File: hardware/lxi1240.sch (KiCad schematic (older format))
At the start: 1 part

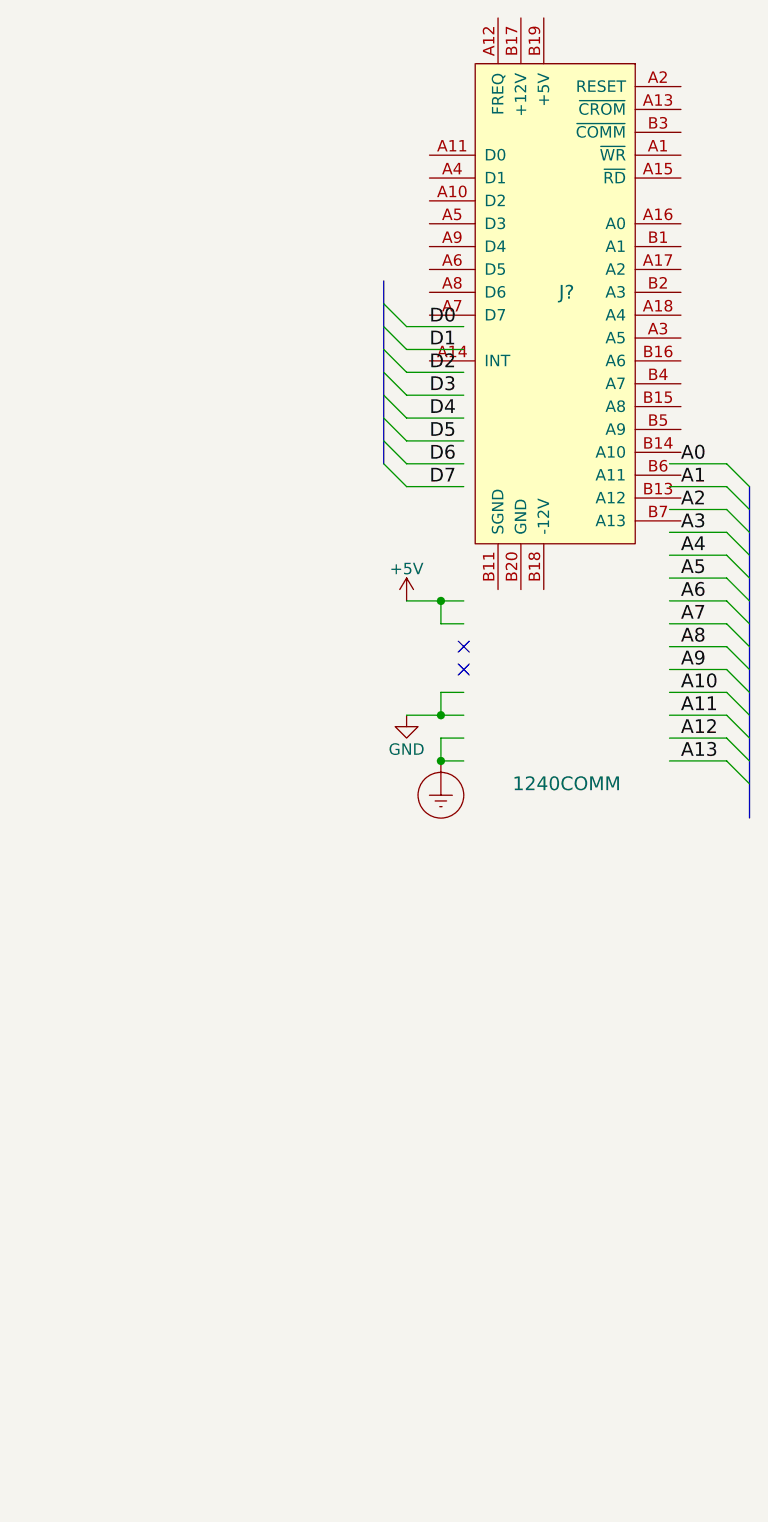
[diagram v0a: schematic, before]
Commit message: Make board-edge symbol compliant with KLC.
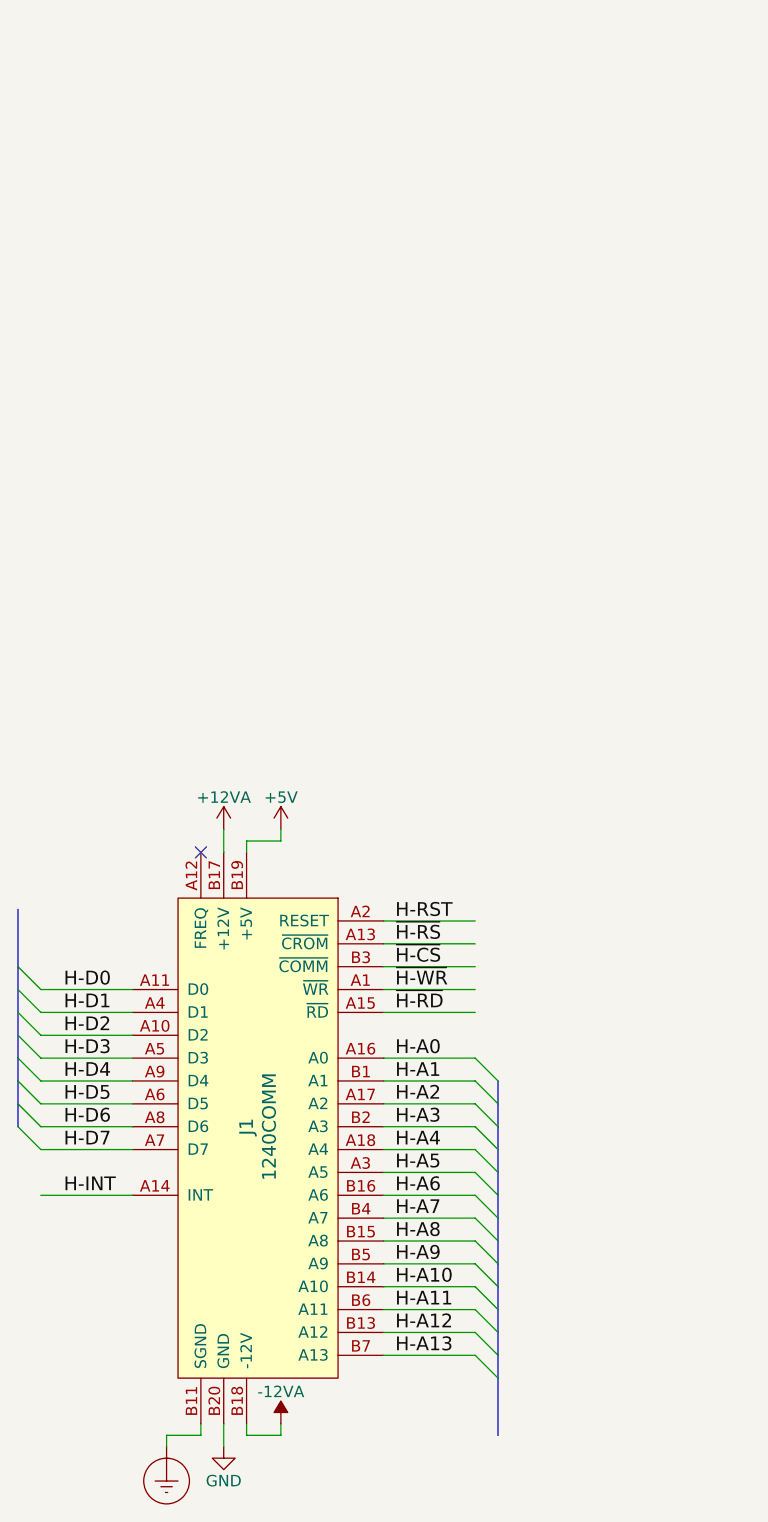
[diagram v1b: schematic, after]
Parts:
- removed J?: 1240COMM, symbol 1240COMM
- added J1: 1240COMM, symbol 1240COMM
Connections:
- net labels added: +12VA, -12VA, H-A0, H-A1, H-A10, H-A11, H-A12, H-A13, H-A2, H-A3, H-A4, H-A5, H-A6, H-A7, H-A8, H-A9, H-D0, H-D1, H-D2, H-D3, H-D4, H-D5, H-D6, H-D7, H-INT, H-RST, ~H-CS, ~H-RD, ~H-RS, ~H-WR
- net labels removed: A0, A1, A10, A11, A12, A13, A2, A3, A4, A5, A6, A7, A8, A9, D0, D1, D2, D3, D4, D5, D6, D7
- wire segments 31 -> 39
- no-connect marks 2 -> 1

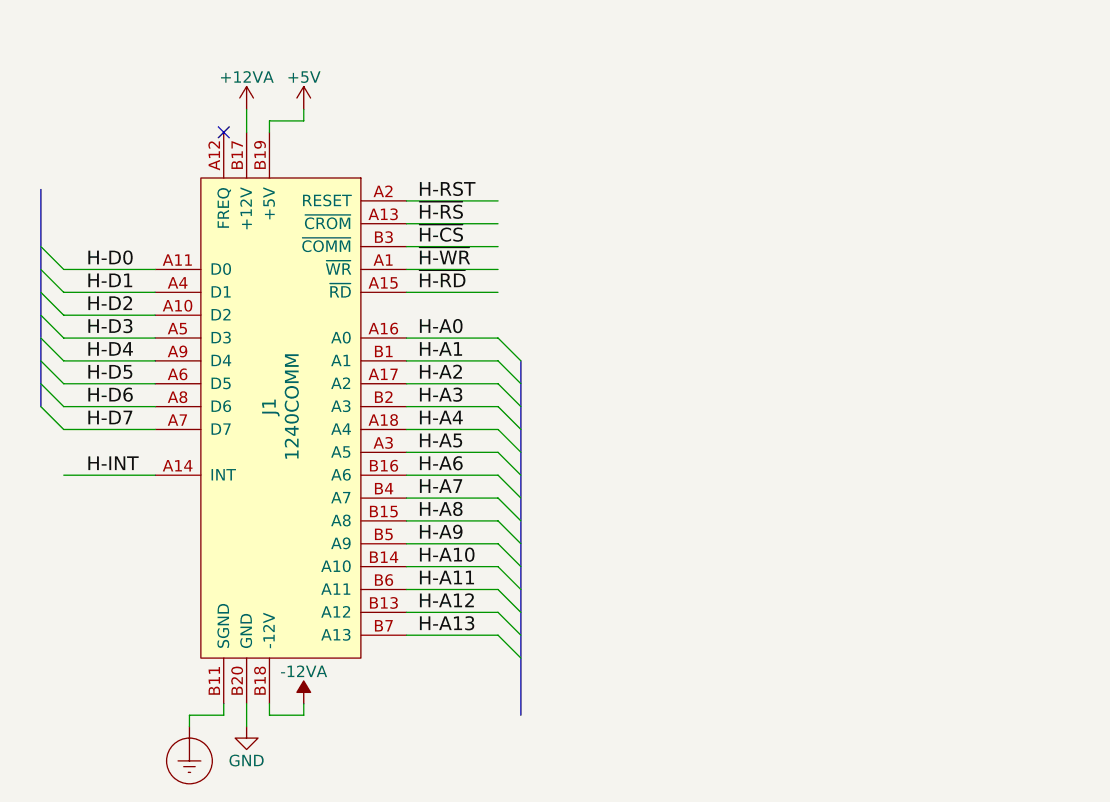
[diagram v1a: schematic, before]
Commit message: Add a breakout header for the board edge connector.
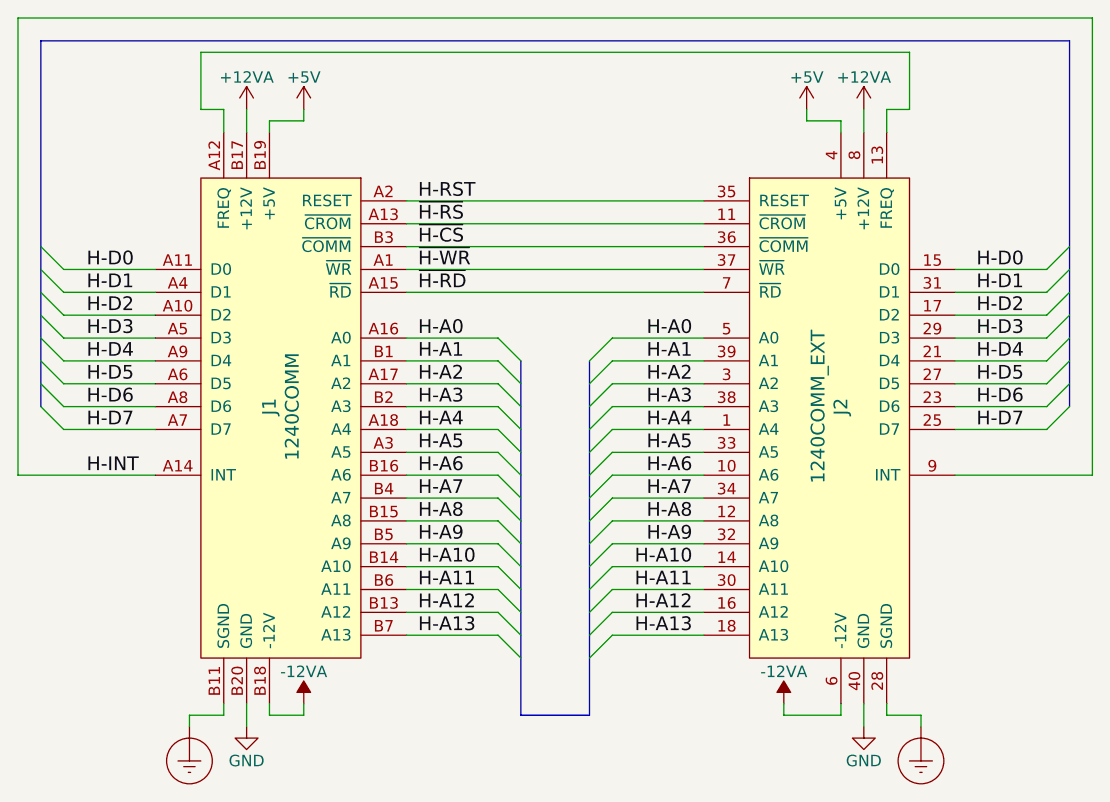
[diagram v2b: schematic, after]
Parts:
- added J2: 1240COMM_EXT, Pin_Headers:Pin_Header_Straight_1x20_Pitch2.54mm, symbol 1240COMM_EXT
- J1: footprint (none) -> 1240comm:1240COMM
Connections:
- wire segments 39 -> 83
- no-connect marks 1 -> 0

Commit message: Add mounting holes with protective ground.
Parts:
- added H1, H2, H3, H4: Mount, Mounting_Holes:MountingHole_3.2mm_M3_Pad, symbol Screw_Terminal_01x01
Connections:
- net Earth_Protective: now also H1.1 (Pin_1), H2.1 (Pin_1), H3.1 (Pin_1), H4.1 (Pin_1)
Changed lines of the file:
@@
 Wire Wire Line
 	5300 6300 4700 6300
+$Comp
+L Screw_Terminal_01x01 H1
+U 1 1 59FEB8E7
+P 6350 5800
+F 0 "H1" H 6350 5900 50  0000 C CNN
+F 1 "Mount" H 6350 5700 50  0000 C CNN
+F 2 "Mounting_Holes:MountingHole_3.2mm_M3_Pad" H 6350 5800 50  0001 C CNN
+F 3 "" H 6350 5800 50  0001 C CNN
+	1    6350 5800
+	1    0    0    -1
+$EndComp
+$Comp
+L Screw_Terminal_01x01 H2
+U 1 1 59FEB959
+P 6350 6100
+F 0 "H2" H 6350 6200 50  0000 C CNN
+F 1 "Mount" H 6350 6000 50  0000 C CNN
+F 2 "Mounting_Holes:MountingHole_3.2mm_M3_Pad" H 6350 6100 50  0001 C CNN
+F 3 "" H 6350 6100 50  0001 C CNN
+	1    6350 6100
+	1    0    0    -1
+$EndComp
+$Comp
+L Screw_Terminal_01x01 H3
+U 1 1 59FEB991
+P 6350 6400
+F 0 "H3" H 6350 6500 50  0000 C CNN
+F 1 "Mount" H 6350 6300 50  0000 C CNN
+F 2 "Mounting_Holes:MountingHole_3.2mm_M3_Pad" H 6350 6400 50  0001 C CNN
+F 3 "" H 6350 6400 50  0001 C CNN
+	1    6350 6400
+	1    0    0    -1
+$EndComp
+$Comp
+L Screw_Terminal_01x01 H4
+U 1 1 59FEB9B8
+P 6350 6700
+F 0 "H4" H 6350 6800 50  0000 C CNN
+F 1 "Mount" H 6350 6600 50  0000 C CNN
+F 2 "Mounting_Holes:MountingHole_3.2mm_M3_Pad" H 6350 6700 50  0001 C CNN
+F 3 "" H 6350 6700 50  0001 C CNN
+	1    6350 6700
+	1    0    0    -1
+$EndComp
+$Comp
+L Earth_Protective #PWR011
+U 1 1 59FEBA57
+P 6050 6950
+F 0 "#PWR011" H 6300 6700 50  0001 C CNN
+F 1 "Earth_Protective" H 6500 6800 50  0001 C CNN
+F 2 "" H 6050 6850 50  0001 C CNN
+F 3 "" H 6050 6850 50  0001 C CNN
+	1    6050 6950
+	1    0    0    -1
+$EndComp
+Wire Wire Line
+	6150 5800 6050 5800
+Wire Wire Line
+	6050 5800 6050 6950
+Wire Wire Line
+	6150 6100 6050 6100
+Connection ~ 6050 6100
+Wire Wire Line
+	6150 6400 6050 6400
+Connection ~ 6050 6400
+Wire Wire Line
+	6150 6700 6050 6700
+Connection ~ 6050 6700
 $EndSCHEMATC

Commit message: Remove pad for key pin in ATA header.
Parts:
- J2: footprint Pin_Headers:Pin_Header_Straight_1x20_Pitch2.54mm -> 1240comm:ATA_HEADER
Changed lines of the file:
@@
 F 0 "J2" V 4200 6000 60  0000 C CNN
 F 1 "1240COMM_EXT" V 4100 6000 60  0000 C CNN
-F 2 "Pin_Headers:Pin_Header_Straight_1x20_Pitch2.54mm" H 4500 7650 60  0001 C CNN
+F 2 "1240comm:ATA_HEADER" H 4500 7650 60  0001 C CNN
 F 3 "" H 4500 7650 60  0001 C CNN
 	1    4100 6000

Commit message: Add CERN OHL license notices.
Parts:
- J2: footprint 1240comm:ATA_HEADER -> (none)
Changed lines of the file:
@@
 encoding utf-8
 Sheet 1 1
-Title ""
+Title "LXI Comm Pack for Tektronix 1240"
 Date ""
 Rev ""
-Comp ""
-Comment1 ""
-Comment2 ""
+Comp "© 2017 Sam Hanes <sam@maltera.com>"
+Comment1 "Licensed under CERN OHL v1.2 or later"
+Comment2 "https://github.com/Elemecca/lxi1240"
 Comment3 ""
 Comment4 ""
@@
 Wire Wire Line
 	1850 7350 1850 7300
-$Comp
-L 1240COMM_EXT J2
-U 1 1 59FE6D32
-P 4100 6000
-F 0 "J2" V 4200 6000 60  0000 C CNN
-F 1 "1240COMM_EXT" V 4100 6000 60  0000 C CNN
-F 2 "1240comm:ATA_HEADER" H 4500 7650 60  0001 C CNN
-F 3 "" H 4500 7650 60  0001 C CNN
-	1    4100 6000
-	1    0    0    -1
-$EndComp
 Entry Wire Line
 	3200 5700 3100 5800
@@
 	6150 6700 6050 6700
 Connection ~ 6050 6700
+$Comp
+L 1240COMM_EXT J2
+U 1 1 59FF3E76
+P 4100 6000
+F 0 "J2" V 4200 6000 60  0000 C CNN
+F 1 "1240COMM_EXT" V 4100 6000 60  0000 C CNN
+F 2 "" H 4500 7650 60  0001 C CNN
+F 3 "" H 4500 7650 60  0001 C CNN
+	1    4100 6000
+	1    0    0    -1
+$EndComp
 $EndSCHEMATC

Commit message: Update board for more accurate measurements of the original.
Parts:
- H1, H2, H3, H4: footprint Mounting_Holes:MountingHole_3.2mm_M3_Pad -> 1240comm:MountingHole_140mil_Pad
- J2: footprint (none) -> 1240comm:ATA_HEADER
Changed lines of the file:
@@
 F 0 "H1" H 6350 5900 50  0000 C CNN
 F 1 "Mount" H 6350 5700 50  0000 C CNN
-F 2 "Mounting_Holes:MountingHole_3.2mm_M3_Pad" H 6350 5800 50  0001 C CNN
+F 2 "1240comm:MountingHole_140mil_Pad" H 6350 5800 50  0001 C CNN
 F 3 "" H 6350 5800 50  0001 C CNN
 	1    6350 5800
@@
 F 0 "H2" H 6350 6200 50  0000 C CNN
 F 1 "Mount" H 6350 6000 50  0000 C CNN
-F 2 "Mounting_Holes:MountingHole_3.2mm_M3_Pad" H 6350 6100 50  0001 C CNN
+F 2 "1240comm:MountingHole_140mil_Pad" H 6350 6100 50  0001 C CNN
 F 3 "" H 6350 6100 50  0001 C CNN
 	1    6350 6100
@@
 F 0 "H3" H 6350 6500 50  0000 C CNN
 F 1 "Mount" H 6350 6300 50  0000 C CNN
-F 2 "Mounting_Holes:MountingHole_3.2mm_M3_Pad" H 6350 6400 50  0001 C CNN
+F 2 "1240comm:MountingHole_140mil_Pad" H 6350 6400 50  0001 C CNN
 F 3 "" H 6350 6400 50  0001 C CNN
 	1    6350 6400
@@
 F 0 "H4" H 6350 6800 50  0000 C CNN
 F 1 "Mount" H 6350 6600 50  0000 C CNN
-F 2 "Mounting_Holes:MountingHole_3.2mm_M3_Pad" H 6350 6700 50  0001 C CNN
+F 2 "1240comm:MountingHole_140mil_Pad" H 6350 6700 50  0001 C CNN
 F 3 "" H 6350 6700 50  0001 C CNN
 	1    6350 6700
@@
 F 0 "J2" V 4200 6000 60  0000 C CNN
 F 1 "1240COMM_EXT" V 4100 6000 60  0000 C CNN
-F 2 "" H 4500 7650 60  0001 C CNN
+F 2 "1240comm:ATA_HEADER" H 4500 7650 60  0001 C CNN
 F 3 "" H 4500 7650 60  0001 C CNN
 	1    4100 6000

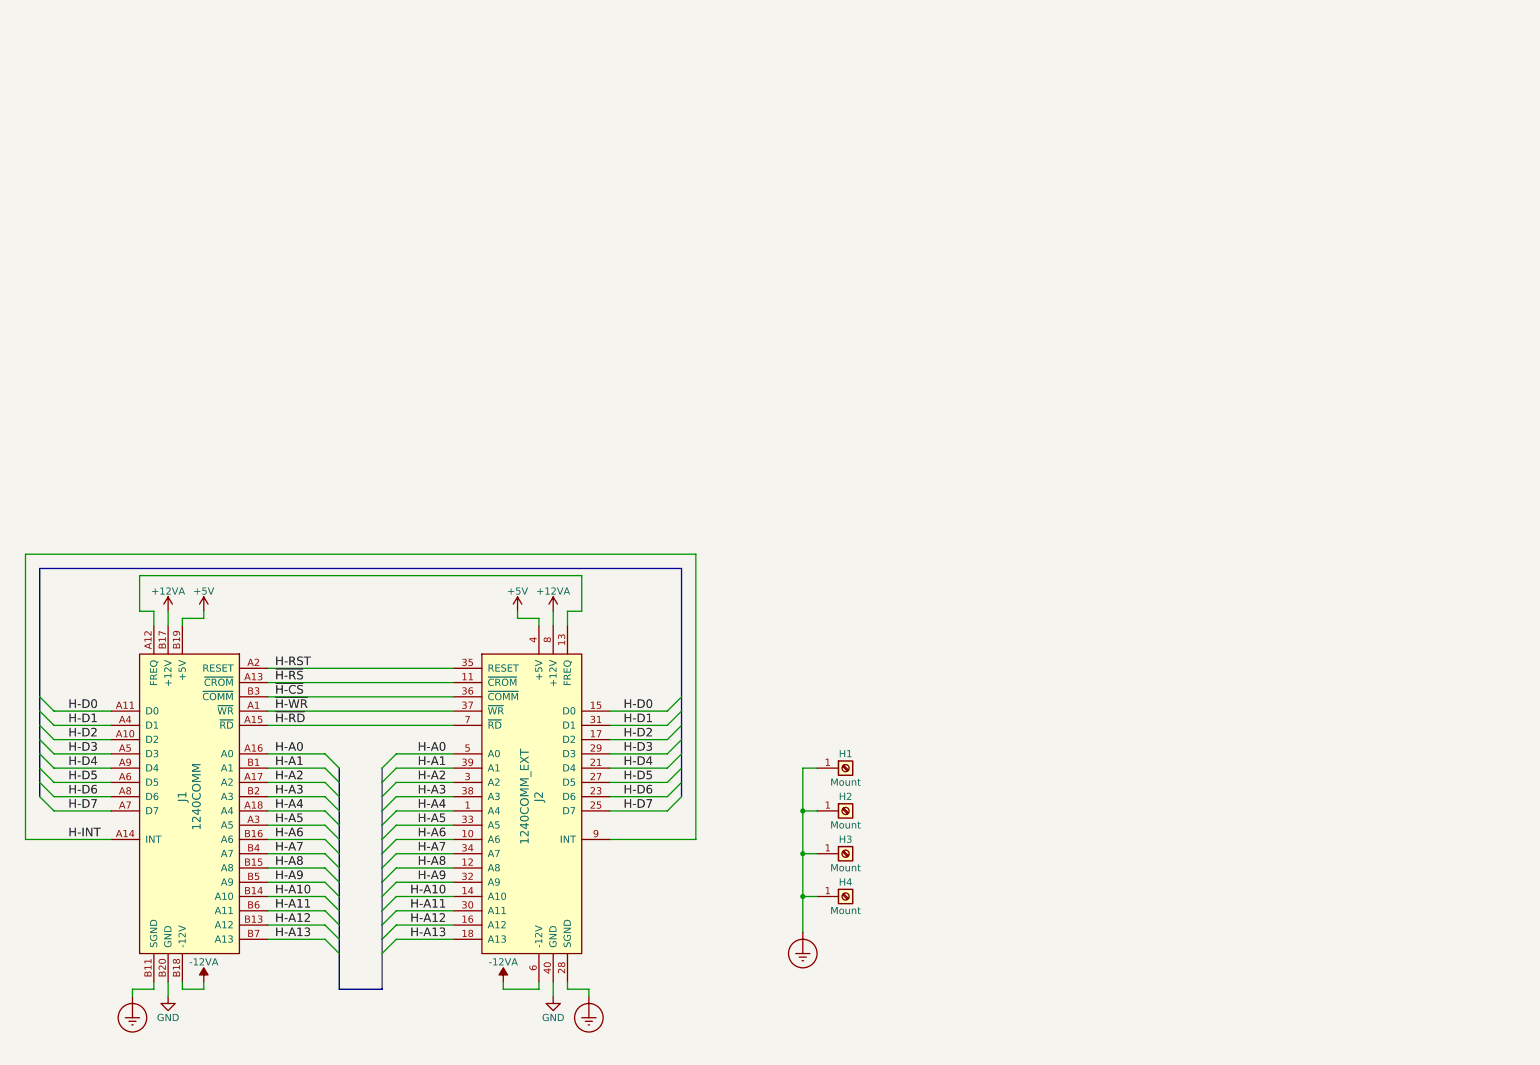
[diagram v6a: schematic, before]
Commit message: Add a PIC micro to manage the host bus.
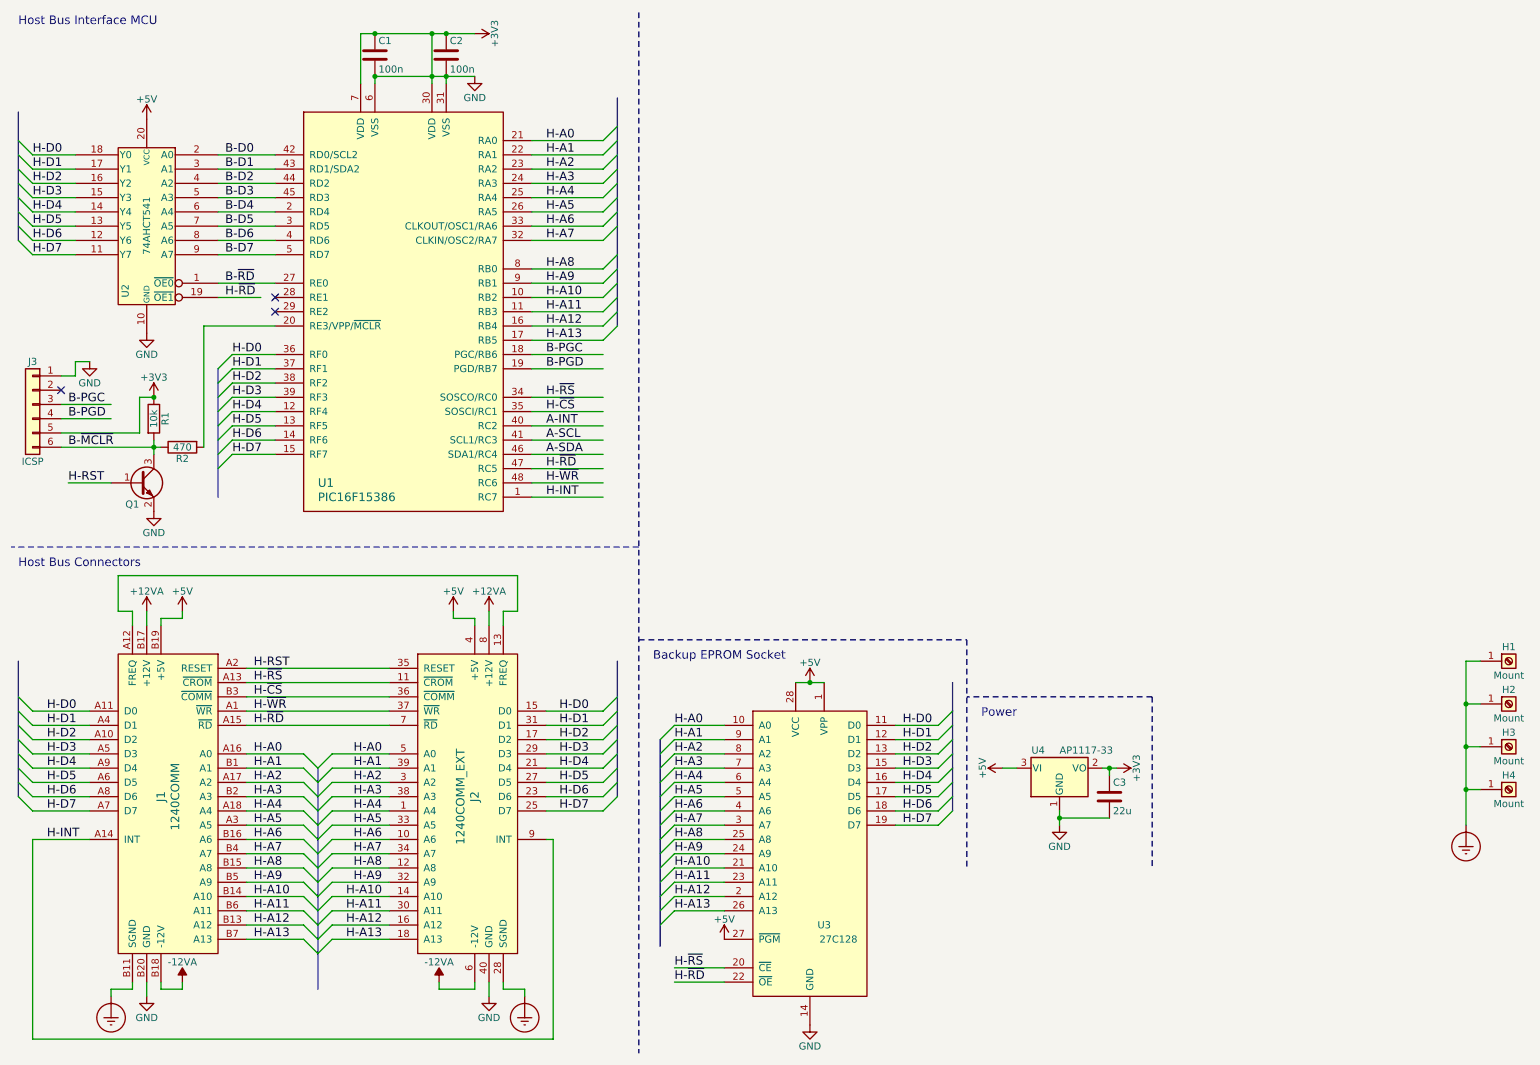
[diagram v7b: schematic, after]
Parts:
- added C1, C2: 100n, Capacitors_SMD:C_0805_HandSoldering, symbol C
- added C3: 22u, Capacitors_SMD:C_0805_HandSoldering, symbol C
- added J3: ICSP, Pin_Headers:Pin_Header_Straight_1x06_Pitch2.54mm, symbol Conn_01x06
- added Q1: Q_NPN_BEC, symbol Q_NPN_BEC
- added R1: 10k, Resistors_SMD:R_0805_HandSoldering, symbol R
- added R2: 470, Resistors_SMD:R_0805_HandSoldering, symbol R
- added U1: PIC16F15386, Housings_QFP:TQFP-48_7x7mm_Pitch0.5mm, symbol PIC16F1538X
- added U2: 74AHCT541, Housings_SSOP:TSSOP-20_4.4x6.5mm_Pitch0.65mm, symbol 74AHCT541
- added U3: 27C128, symbol 27C128
- added U4: AP1117-33, TO_SOT_Packages_SMD:SOT-223-3_TabPin2, symbol AP1117-33
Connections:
- net labels added: +3V3, A-INT, A-SCL, A-SDA, B-D0, B-D1, B-D2, B-D3, B-D4, B-D5, B-D6, B-D7, B-PGC, B-PGD, B-~MCLR, B-~RD, H-~CS, H-~RD, H-~RS, H-~WR
- net labels removed: ~H-CS, ~H-RD, ~H-RS, ~H-WR
- wire segments 88 -> 187
- no-connect marks 0 -> 3
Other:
- note added: "Backup EPROM Socket"
- note added: "Host Bus Connectors"
- note added: "Host Bus Interface MCU"
- note added: "Power"
- moved on the sheet: H1, H2, H3, H4, J1
